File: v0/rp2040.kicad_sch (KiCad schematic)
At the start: 25 parts, among them J2 Conn_01x03_Pin, U3 RP2040, U4 W25Q16JVUXIQ, Y1 12MHZ-3225-24GND

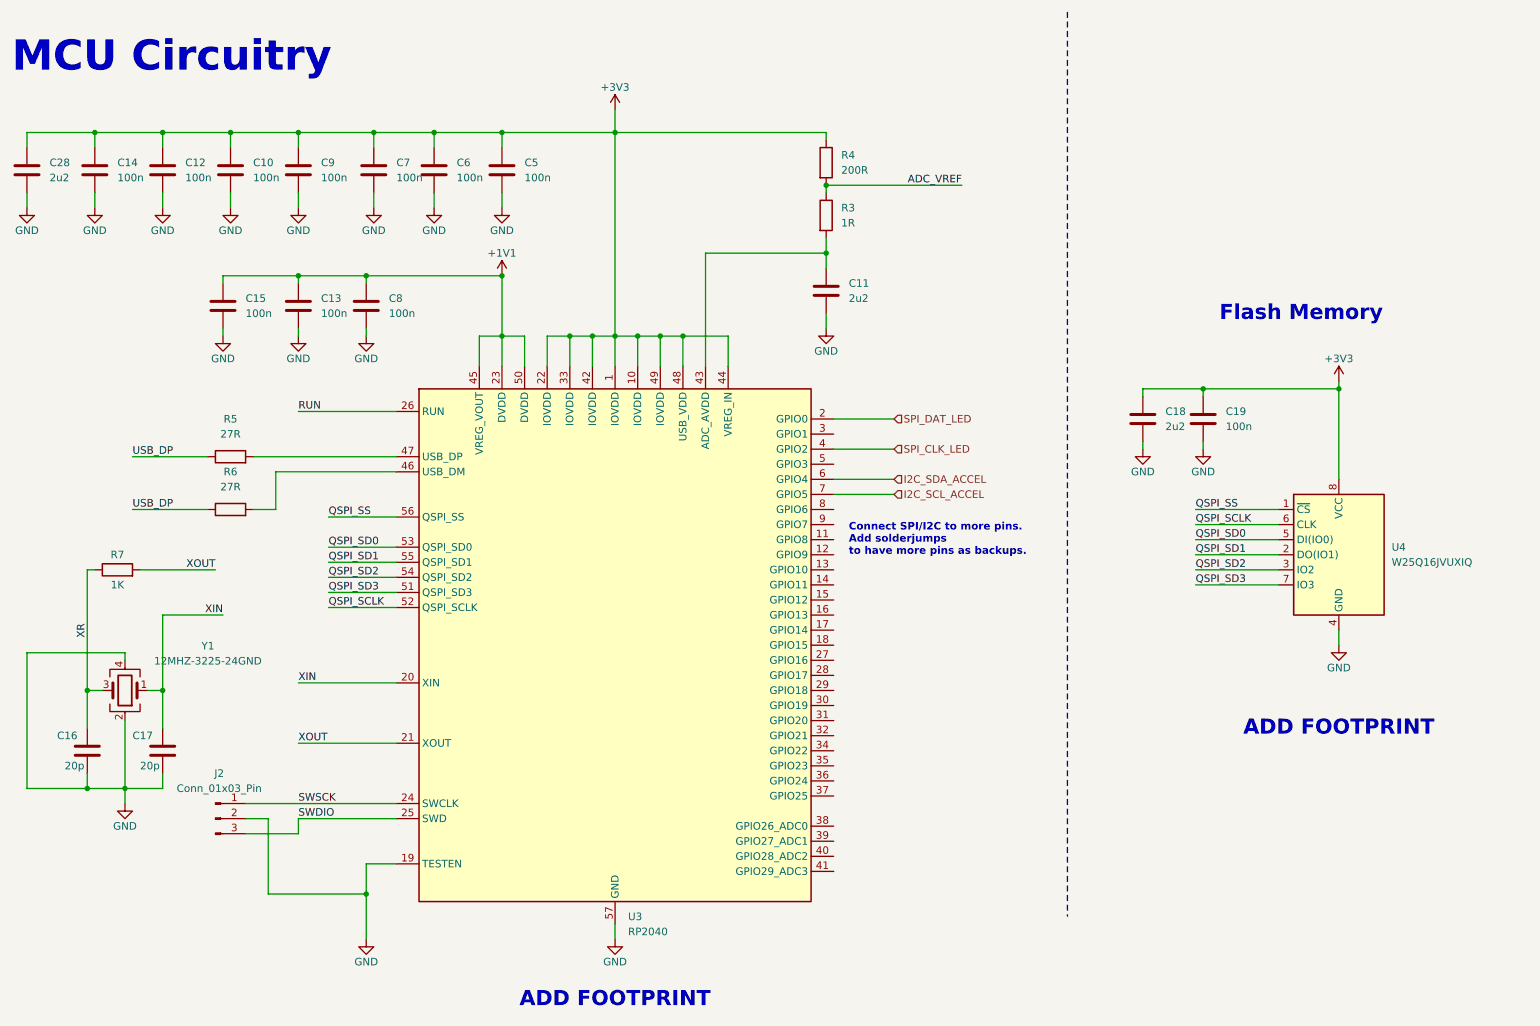
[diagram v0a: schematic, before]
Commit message: Picked new LED driver TLC59116, conected over I2C (instead of the previous one that used SPI), increased number of LEDs from 24 to 32.
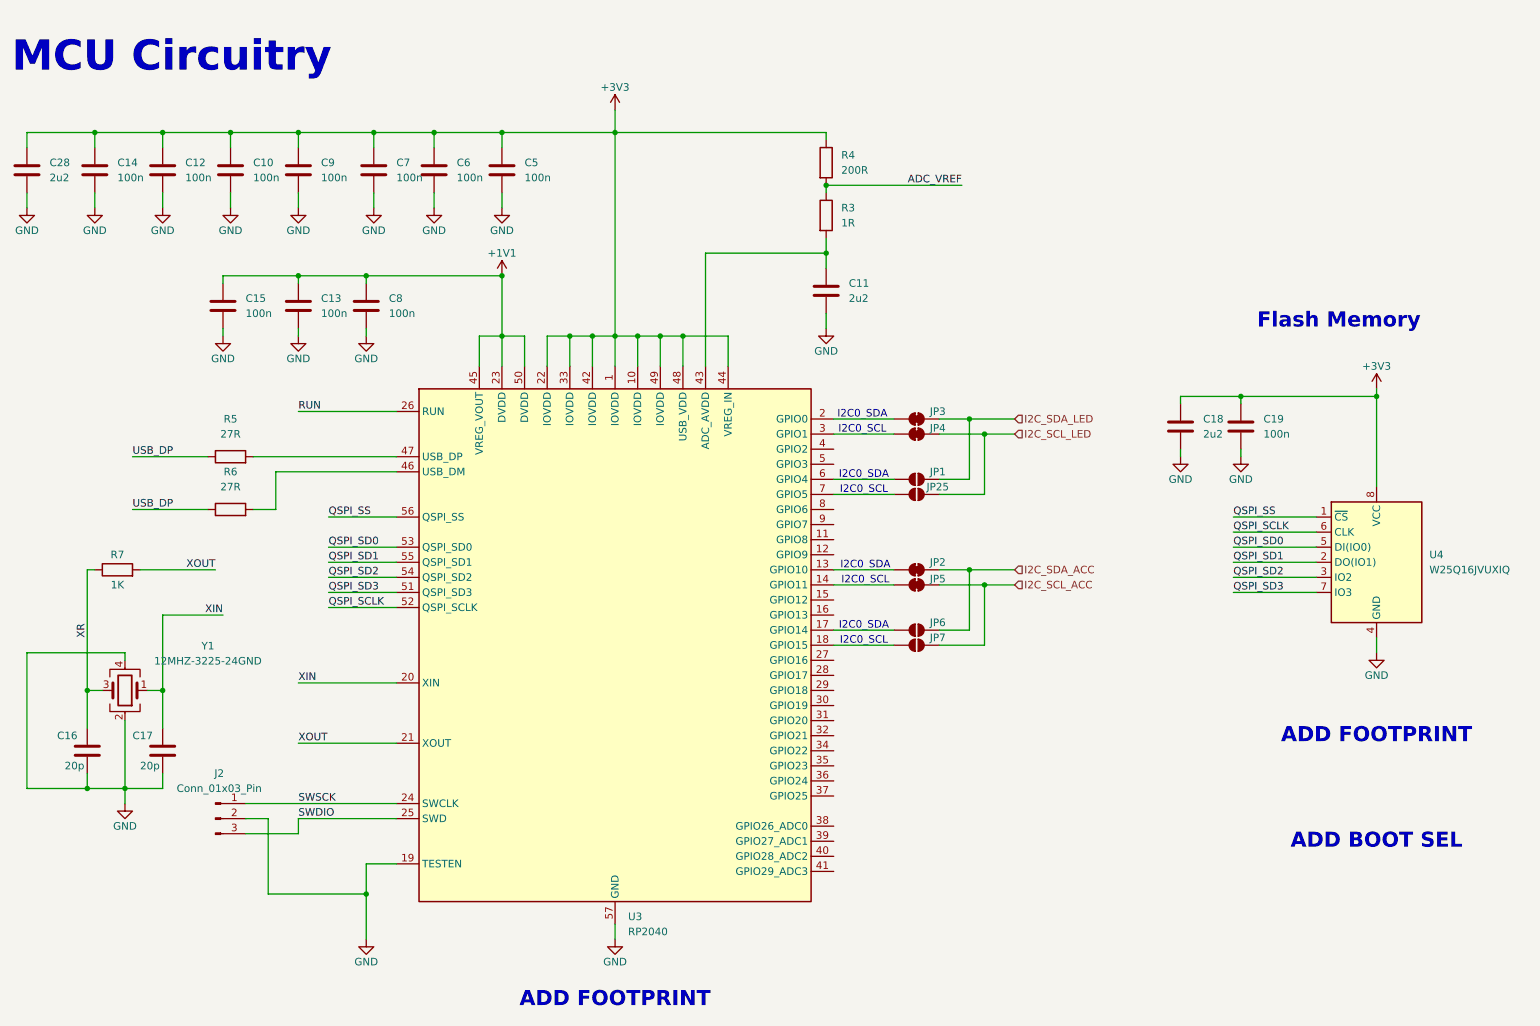
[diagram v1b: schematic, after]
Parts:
- added JP1, JP25, JP6, JP7: SolderJumper_2_Open, symbol Jumper:SolderJumper_2_Open
- added JP2, JP3, JP4, JP5: SolderJumper_2_Bridged, symbol Jumper:SolderJumper_2_Bridged
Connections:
- net at U3.13 (GPIO10): now also JP2.1 (A)
- net at U3.14 (GPIO11): now also JP5.1 (A)
- net at U3.17 (GPIO14): now also JP6.1 (A)
- net at U3.18 (GPIO15): now also JP7.1 (A)
- net at U3.3 (GPIO1): now also JP4.1 (A)
- net I2C_SCL_ACCEL: no longer names the net of U3.7 (GPIO5)
- net I2C_SCL_ACCEL: now also JP25.1 (A)
- net I2C_SDA_ACCEL: no longer names the net of U3.6 (GPIO4)
- net I2C_SDA_ACCEL: now also JP1.1 (A)
- net SPI_CLK_LED: no longer names the net of U3.4 (GPIO2)
- net SPI_DAT_LED: no longer names the net of U3.2 (GPIO0)
- net SPI_DAT_LED: now also JP3.1 (A)
- new net I2C_SCL_ACC: JP5.2 (B), JP7.2 (B)
- new net I2C_SCL_LED: JP25.2 (B), JP4.2 (B)
- new net I2C_SDA_ACC: JP2.2 (B), JP6.2 (B)
- new net I2C_SDA_LED: JP1.2 (B), JP3.2 (B)
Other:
- note added: "ADD BOOT SEL"
- note added: "I2C0_SCL"
- note added: "I2C0_SDA"
- note removed: "Connect SPI/I2C to more pins. Add solderjumps to have more pins as backups."
- moved on the sheet: C18, C19, U4
